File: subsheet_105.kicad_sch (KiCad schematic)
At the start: 39 parts, among them T01 BC547B, T02 BC547B, T03 BC547B

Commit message: update comments in cartridge
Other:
- title: Conversion du Thomson MO5 — Unité centrale v1 -> Conversion du Thomson MO5 — Unité centrale v2
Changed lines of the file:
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@@
   (paper "A4" portrait)
   (title_block
-    (title "Conversion du Thomson MO5 — Unité centrale v1")
-    (date "2024-12-30")
-    (rev "v1.0.0-rc2")
+    (title "Conversion du Thomson MO5 — Unité centrale v2")
+    (date "2025-02-08")
+    (rev "v2.0.0-alpha")
     (comment 1 "http://github.com/sporniket/kicad-conversions--thomson-mo5--v1")
-    (comment 3 "Gate Array Motorola MCA 1300 ALS")
-    (comment 4 "Reference : POP5001 501994-01")
+    (comment 3 "Gate Array EFCIS")
   )
   (junction (at 114.3 241.3) (diameter 0) (color 0 0 0 0)

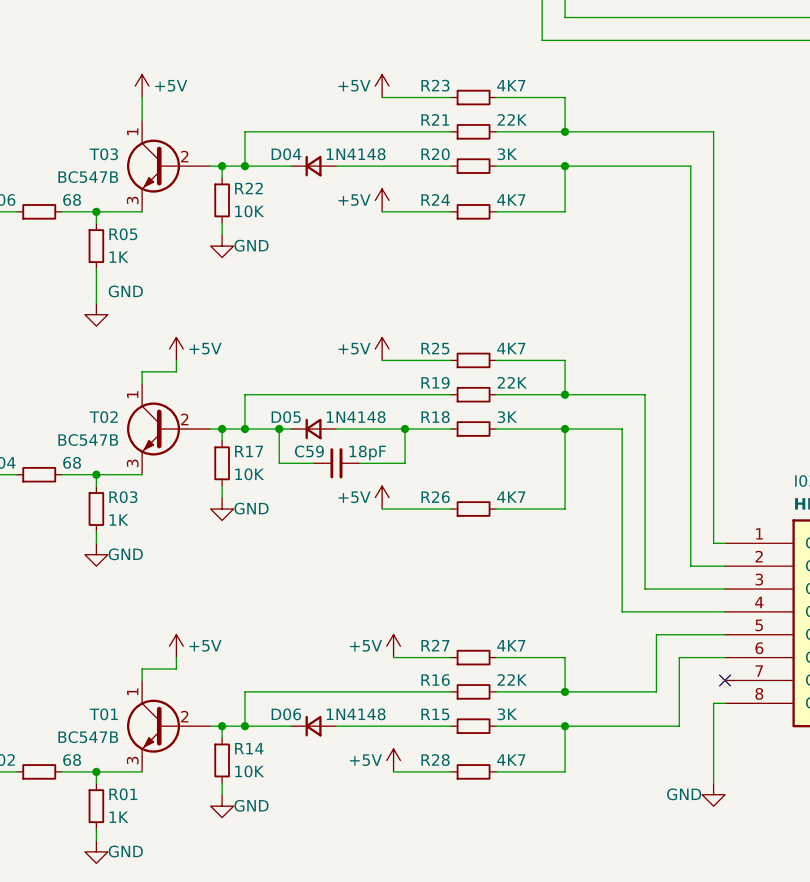
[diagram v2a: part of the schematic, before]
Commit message: Partially #20 : added C62, C63
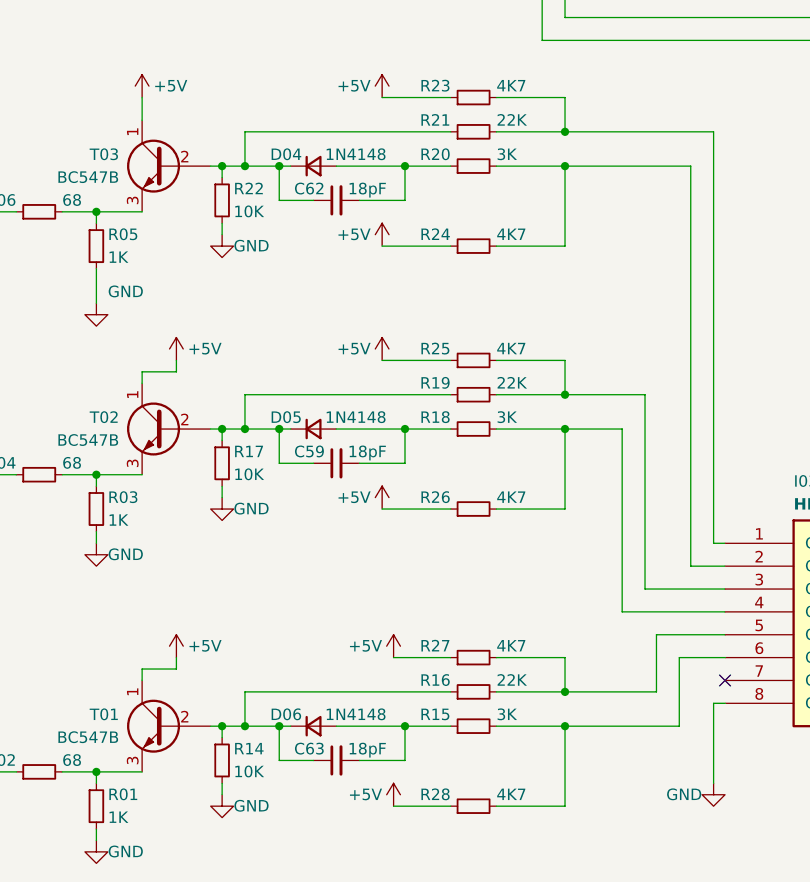
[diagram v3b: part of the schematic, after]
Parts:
- added C62, C63: 18pF, commons-passives_THT:Passive_THT_capacitor_mlcc_W2.54mm_L5.08mm, symbol Device:C_Small
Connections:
- net at D06.1 (K), R14.1, R16.1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: now also C63.1
- net at D04.1 (K), R21.1, R22.1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: now also C62.1
- net at D04.2 (A), R20.1: now also C62.2
- net at D06.2 (A), R15.1: now also C63.2
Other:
- moved on the sheet: R24, R28

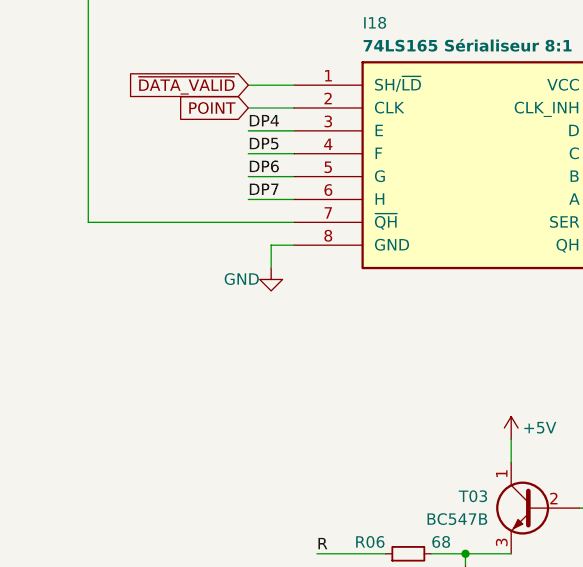
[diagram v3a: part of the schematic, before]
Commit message: Done #20 : missing capacitors C65, C69, C70, C80 (footprints on PCB, not found on schematics)
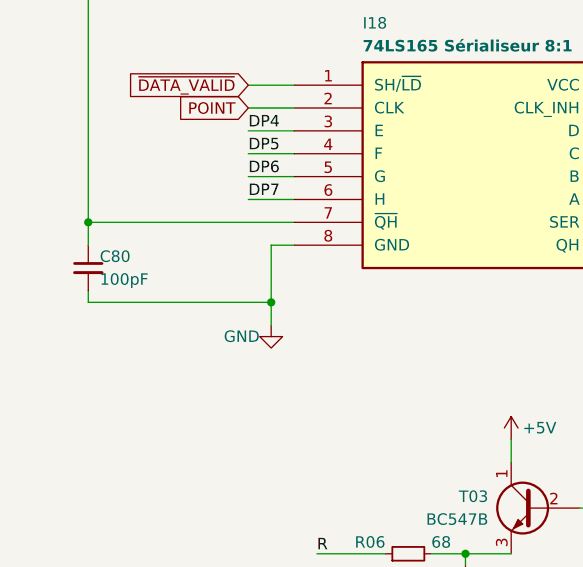
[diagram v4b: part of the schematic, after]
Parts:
- added C80: 100pF, commons-passives_THT:Passive_THT_capacitor_mlcc_W2.54mm_L5.08mm, symbol Device:C_Small
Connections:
- net GND: now also C80.2
- net at I06.1 (~{OE1}), I18.7 (~{QH}): now also C80.1
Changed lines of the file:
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@@
   (junction (at 114.3 237.49) (diameter 0) (color 0 0 0 0)
   )
+  (junction (at 20.32 147.32) (diameter 0) (color 0 0 0 0)
+  )
   (junction (at 114.3 204.47) (diameter 0) (color 0 0 0 0)
   )
@@
   )
   (junction (at 93.98 78.74) (diameter 0) (color 0 0 0 0)
+  )
+  (junction (at 40.64 156.21) (diameter 0) (color 0 0 0 0)
   )
   (junction (at 78.74 241.3) (diameter 0) (color 0 0 0 0)
@@
     (stroke (width 0) (type default))
   )
-  (wire (pts (xy 40.64 152.4) (xy 40.64 149.86))
+  (wire (pts (xy 40.64 158.75) (xy 40.64 156.21))
     (stroke (width 0) (type default))
   )
@@
     (stroke (width 0) (type default))
   )
+  (wire (pts (xy 20.32 156.21) (xy 40.64 156.21))
+    (stroke (width 0) (type default))
+  )
   (wire (pts (xy 96.52 208.28) (xy 101.6 208.28))
     (stroke (width 0) (type default))
@@
     (stroke (width 0) (type default))
   )
+  (wire (pts (xy 40.64 156.21) (xy 40.64 149.86))
+    (stroke (width 0) (type default))
+  )
   (wire (pts (xy 95.25 233.68) (xy 101.6 233.68))
     (stroke (width 0) (type default))
@@
     (stroke (width 0) (type default))
   )
+  (wire (pts (xy 20.32 154.94) (xy 20.32 156.21))
+    (stroke (width 0) (type default))
+  )
   (wire (pts (xy 39.37 78.74) (xy 46.99 78.74))
     (stroke (width 0) (type default))
@@
   )
   (wire (pts (xy 114.3 175.26) (xy 130.81 175.26))
+    (stroke (width 0) (type default))
+  )
+  (wire (pts (xy 20.32 147.32) (xy 20.32 149.86))
     (stroke (width 0) (type default))
   )
@@
     )
   )
+  (symbol (lib_id "Device:C_Small") (at 20.32 152.4 0) (unit 1)
+    (in_bom yes) (on_board yes) (dnp no)
+    (property "Reference" "C80" (at 21.59 151.13 0)
+      (effects (font (size 1.27 1.27)) (justify left))
+    )
+    (property "Value" "100pF" (at 21.59 153.67 0)
+      (effects (font (size 1.27 1.27)) (justify left))
+    )
+    (property "Footprint" "commons-passives_THT:Passive_THT_capacitor_mlcc_W2.54mm_L5.08mm" (at 20.32 152.4 0)
+      (effects (font (size 1.27 1.27)) hide)
+    )
+    (property "Datasheet" "~" (at 20.32 152.4 0)
+      (effects (font (size 1.27 1.27)) hide)
+    )
+    (pin "1")
+    (pin "2")
+    (instances
+      (project "UC-50-001"
+        (path "/e63e39d7-6ac0-4ffd-8aa3-1841a4541b55/10b20128-1f32-45c7-94f3-33002744903c"
+          (reference "C80") (unit 1)
+        )
+      )
+    )
+  )
   (symbol (lib_id "power:GND") (at 171.45 208.28 0) (unit 1)
     (in_bom yes) (on_board yes) (dnp no)
@@
     )
   )
-  (symbol (lib_id "power:GND") (at 40.64 152.4 0) (unit 1)
-    (in_bom yes) (on_board yes) (dnp no)
-    (property "Reference" "#PWR0229" (at 40.64 158.75 0)
-      (effects (font (size 1.27 1.27)) hide)
-    )
-    (property "Value" "GND" (at 39.37 153.67 0)
-      (effects (font (size 1.27 1.27)) (justify right))
-    )
-    (property "Footprint" "" (at 40.64 152.4 0)
-      (effects (font (size 1.27 1.27)) hide)
-    )
-    (property "Datasheet" "" (at 40.64 152.4 0)
-      (effects (font (size 1.27 1.27)) hide)
-    )
+  (symbol (lib_id "power:GND") (at 40.64 158.75 0) (unit 1)
+    (in_bom yes) (on_board yes) (dnp no)
+    (property "Reference" "#PWR0229" (at 40.64 165.1 0)
+      (effects (font (size 1.27 1.27)) hide)
+    )
+    (property "Value" "GND" (at 39.37 160.02 0)
+      (effects (font (size 1.27 1.27)) (justify right))
+    )
+    (property "Footprint" "" (at 40.64 158.75 0)
+      (effects (font (size 1.27 1.27)) hide)
+    )
+    (property "Datasheet" "" (at 40.64 158.75 0)
+      (effects (font (size 1.27 1.27)) hide)
+    )

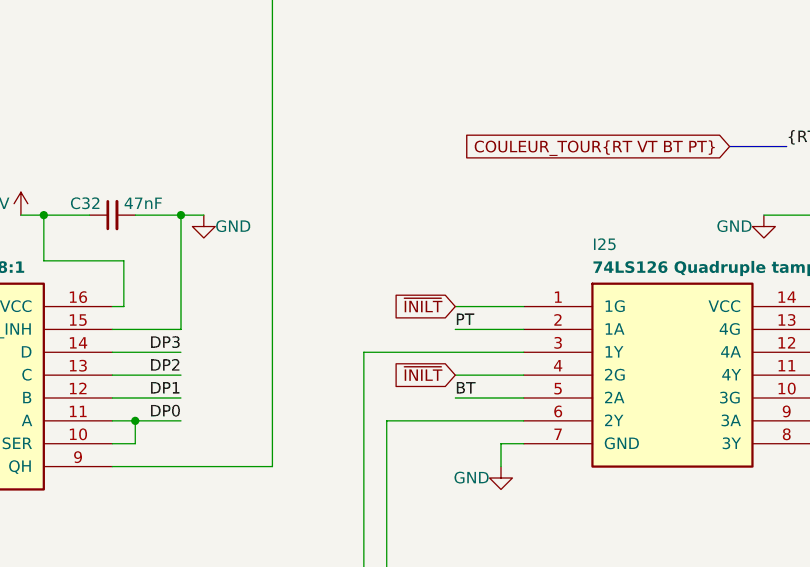
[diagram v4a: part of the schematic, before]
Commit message: Fixed #21 : missing C58
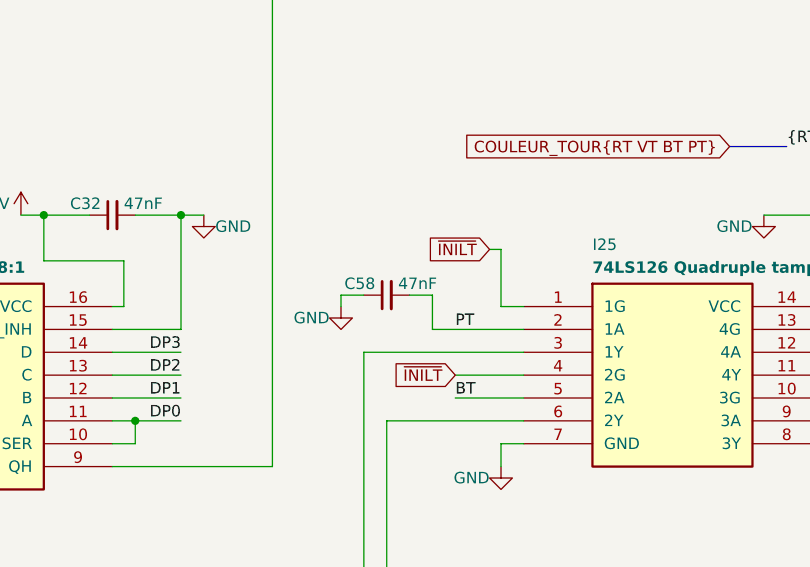
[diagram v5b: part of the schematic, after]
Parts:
- added C58: 47nF, commons-passives_THT:Passive_THT_capacitor_mlcc_W2.54mm_L5.08mm, symbol Device:C_Small
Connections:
- net GND: now also C58.1
- net PT: now also C58.2
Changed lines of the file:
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@@
     (stroke (width 0) (type default))
   )
-  (wire (pts (xy 121.92 134.62) (xy 129.54 134.62))
+  (wire (pts (xy 119.38 134.62) (xy 129.54 134.62))
     (stroke (width 0) (type default))
   )
@@
     (stroke (width 0) (type default))
   )
+  (wire (pts (xy 109.22 130.81) (xy 111.76 130.81))
+    (stroke (width 0) (type default))
+  )
   (wire (pts (xy 162.56 142.24) (xy 170.18 142.24))
     (stroke (width 0) (type default))
@@
     (stroke (width 0) (type default))
   )
+  (wire (pts (xy 127 125.73) (xy 127 132.08))
+    (stroke (width 0) (type default))
+  )
   (wire (pts (xy 168.91 208.28) (xy 168.91 223.52))
     (stroke (width 0) (type default))
@@
     (stroke (width 0) (type default))
   )
+  (wire (pts (xy 116.84 130.81) (xy 119.38 130.81))
+    (stroke (width 0) (type default))
+  )
   (wire (pts (xy 40.64 149.86) (xy 43.18 149.86))
     (stroke (width 0) (type default))
@@
     (stroke (width 0) (type default))
   )
-  (wire (pts (xy 121.92 132.08) (xy 129.54 132.08))
+  (wire (pts (xy 125.73 125.73) (xy 127 125.73))
     (stroke (width 0) (type default))
   )
@@
     (stroke (width 0) (type default))
   )
+  (wire (pts (xy 119.38 130.81) (xy 119.38 134.62))
+    (stroke (width 0) (type default))
+  )
   (wire (pts (xy 128.27 179.07) (xy 114.3 179.07))
     (stroke (width 0) (type default))
@@
     (stroke (width 0) (type default))
   )
+  (wire (pts (xy 127 132.08) (xy 129.54 132.08))
+    (stroke (width 0) (type default))
+  )
   (wire (pts (xy 173.99 121.92) (xy 176.53 121.92))
     (stroke (width 0) (type default))
@@
   )
   (wire (pts (xy 62.23 184.15) (xy 67.31 184.15))
+    (stroke (width 0) (type default))
+  )
+  (wire (pts (xy 109.22 132.08) (xy 109.22 130.81))
     (stroke (width 0) (type default))
   )
@@
     (effects (font (size 1.27 1.27)) (justify right bottom))
   )
-  (global_label "~{INILT}" (shape input) (at 121.92 132.08 180) (fields_autoplaced)
+  (global_label "~{INILT}" (shape input) (at 125.73 125.73 180) (fields_autoplaced)
     (effects (font (size 1.27 1.27)) (justify right))
-    (property "Intersheetrefs" "${INTERSHEET_REFS}" (at 114.9712 132.0006 0)
+    (property "Intersheetrefs" "${INTERSHEET_REFS}" (at 118.7812 125.6506 0)
       (effects (font (size 1.27 1.27)) (justify right) hide)
     )
@@
     )
   )
+  (symbol (lib_id "Device:C_Small") (at 114.3 130.81 90) (unit 1)
+    (in_bom yes) (on_board yes) (dnp no)
+    (property "Reference" "C58" (at 113.03 129.54 90)
+      (effects (font (size 1.27 1.27)) (justify left))
+    )
+    (property "Value" "47nF" (at 115.57 129.54 90)
+      (effects (font (size 1.27 1.27)) (justify right))
+    )
+    (property "Footprint" "commons-passives_THT:Passive_THT_capacitor_mlcc_W2.54mm_L5.08mm" (at 114.3 130.81 0)
+      (effects (font (size 1.27 1.27)) hide)
+    )
+    (property "Datasheet" "~" (at 114.3 130.81 0)
+      (effects (font (size 1.27 1.27)) hide)
+    )
+    (pin "1")
+    (pin "2")
+    (instances
+      (project "UC-50-001"
+        (path "/e63e39d7-6ac0-4ffd-8aa3-1841a4541b55/10b20128-1f32-45c7-94f3-33002744903c"
+          (reference "C58") (unit 1)
+        )
+      )
+    )
+  )
   (symbol (lib_id "power:GND") (at 62.23 254 0) (unit 1)
     (in_bom yes) (on_board yes) (dnp no)
@@
         )
       )
+    )
+  )
+  (symbol (lib_id "power:GND") (at 109.22 132.08 0) (unit 1)
+    (in_bom yes) (on_board yes) (dnp no)
+    (property "Reference" "#PWR034" (at 109.22 138.43 0)
+      (effects (font (size 1.27 1.27)) hide)
+    )
+    (property "Value" "GND" (at 107.95 133.35 0)
+      (effects (font (size 1.27 1.27)) (justify right))
+    )
+    (property "Footprint" "" (at 109.22 132.08 0)
+      (effects (font (size 1.27 1.27)) hide)
+    )
+    (property "Datasheet" "" (at 109.22 132.08 0)
+      (effects (font (size 1.27 1.27)) hide)
+    )
+    (pin "1")
+    (instances
+      (project "UC-50-001"
+        (path "/e63e39d7-6ac0-4ffd-8aa3-1841a4541b55/10b20128-1f32-45c7-94f3-33002744903c"
+          (reference "#PWR034") (unit 1)
+        )
+      )
